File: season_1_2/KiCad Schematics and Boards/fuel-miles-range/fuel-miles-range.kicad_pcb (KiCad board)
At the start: 2 copper layers, 132 x 76 mm, 18 parts, among them J601 Conn_02x06_Top_Bottom, U501 TLC5957RTQ, U502 TLC5957RTQ, U601 MCP2562-E-SN, U602 STM32G0B1CET6N

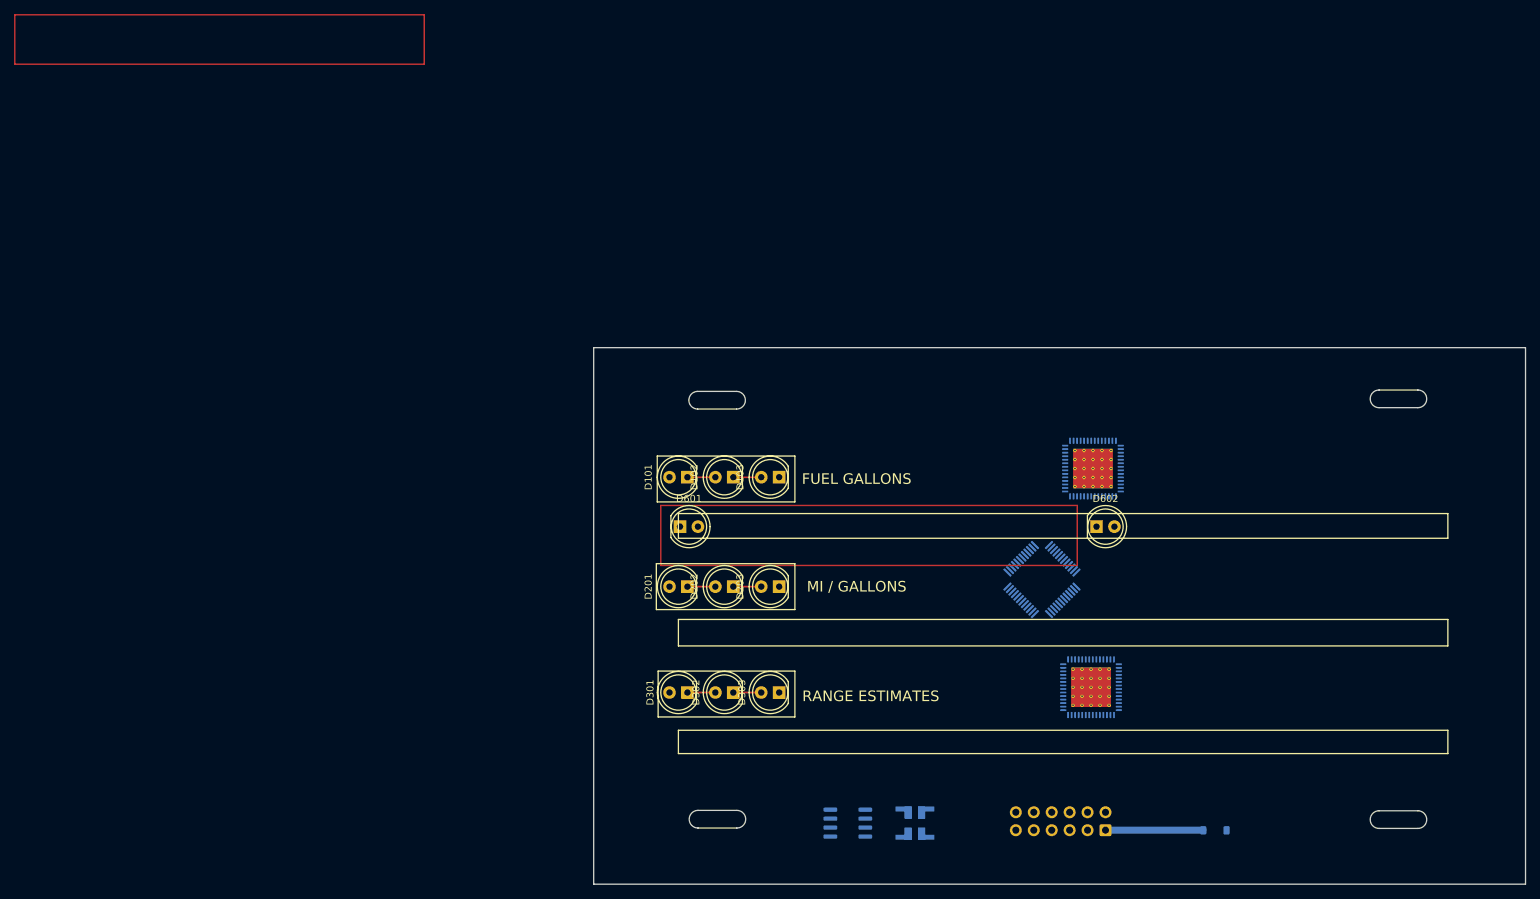
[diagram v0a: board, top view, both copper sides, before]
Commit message: Added lots of electronic devices and routes
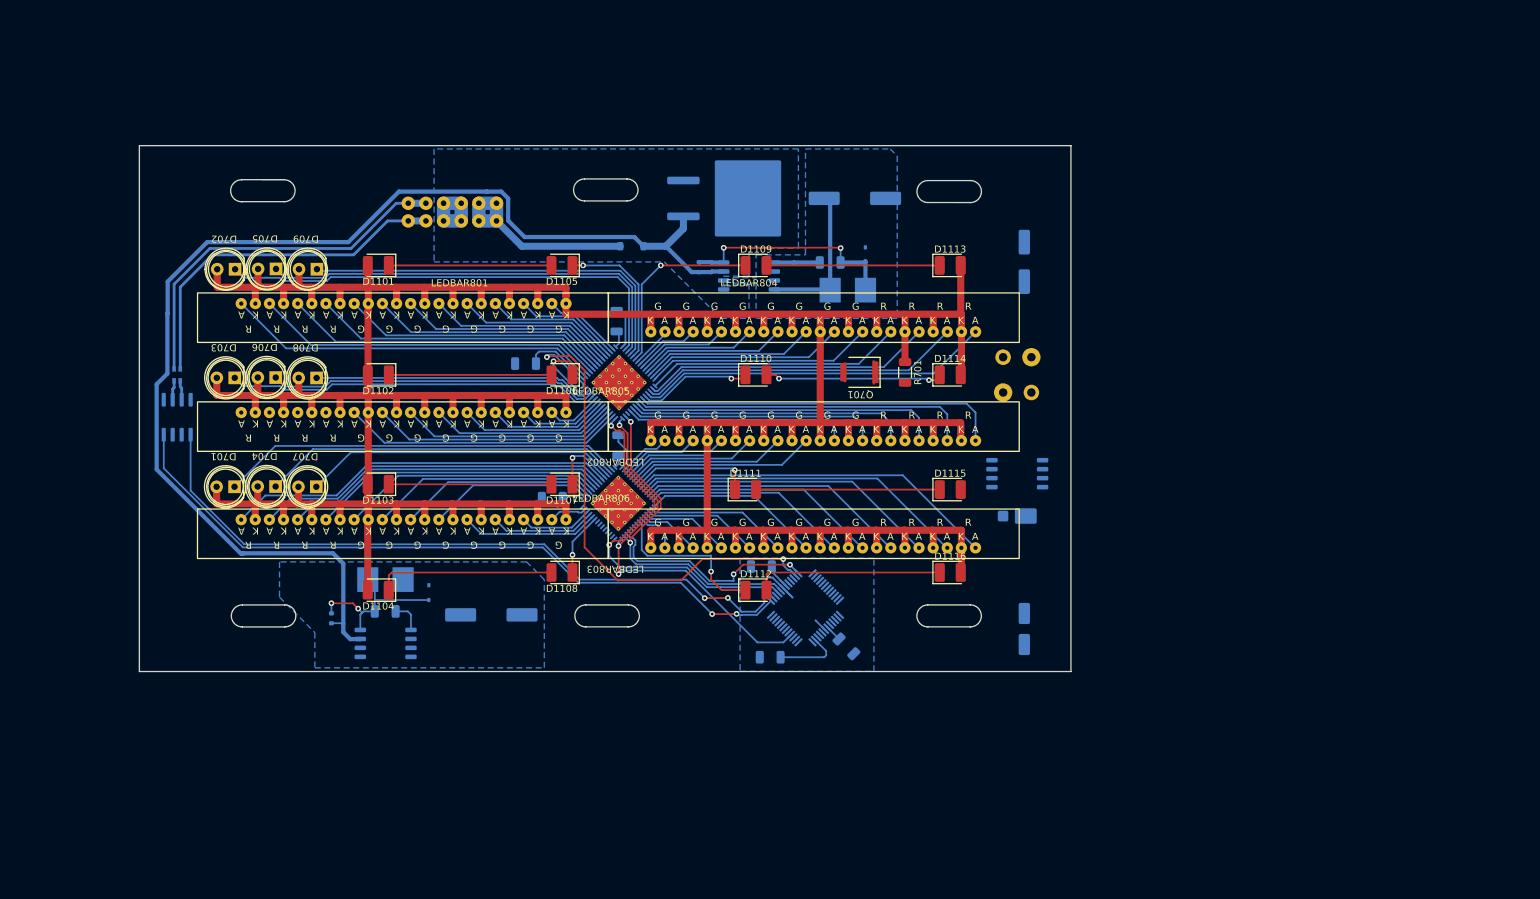
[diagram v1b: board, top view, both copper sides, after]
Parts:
- removed D601, D602: LED, LED_THT:LED_D5.0mm
- removed D603: SM8S24AHE3_A/I, Diode_SMD:D_SOD-123
- removed J601: Conn_02x06_Top_Bottom, Connector_IDC:IDC-Header_2x06_P2.54mm_Vertical
- removed the U501 at (152.7, 64.3)
- removed U502: TLC5957RTQ, Package_DFN_QFN:QFN-56-1EP_8x8mm_P0.5mm_EP5.6x5.6mm_ThermalVias
- added C203: 0.01µF/50V, Capacitor_SMD:C_1206_3216Metric, B.Cu at (115.5, 35.1)
- added C206: 47µF/6,3V, Capacitor_SMD:CP_Elec_10x12.6, B.Cu at (119.0, 26.0)
- added C301: 0.01µF/50V, Capacitor_SMD:C_1206_3216Metric, B.Cu at (52.5, 84.5)
- added C303: 100µF/6,3V, Capacitor_SMD:CP_Elec_10x12.6, B.Cu at (67.5, 85.0)
- added C401: 10µF/25V, Capacitor_SMD:CP_Elec_6.3x5.9, B.Cu at (143.0, 35.0)
- added C402: 47µF/6,3V, Capacitor_SMD:CP_Elec_5x5.7, B.Cu at (143.0, 87.0)
- added C501: 100n, Capacitor_SMD:C_1206_3216Metric, B.Cu at (117.8, 89.5)
- added C502: 100n, Capacitor_SMD:C_1206_3216Metric, B.Cu at (105.8, 78.2)
- added C503: 100n, Capacitor_SMD:C_1206_3216Metric, B.Cu at (107.0, 91.0)
- added C901: 100n, Capacitor_SMD:C_1206_3216Metric, B.Cu at (72.3, 49.4)
- added C902: 100n, Capacitor_SMD:C_1206_3216Metric, B.Cu at (76.1, 68.5)
- added D1101: LED, LED_SMD:LED_1210_3225Metric_Pad1.42x2.65mm_HandSolder, F.Cu at (51.5, 35.5)
- added D1102: LED, LED_SMD:LED_1210_3225Metric_Pad1.42x2.65mm_HandSolder, F.Cu at (51.5, 51.0)
- added D1103: LED, LED_SMD:LED_1210_3225Metric_Pad1.42x2.65mm_HandSolder, F.Cu at (51.5, 66.5)
- added D1104: LED, LED_SMD:LED_1210_3225Metric_Pad1.42x2.65mm_HandSolder, F.Cu at (51.5, 81.5)
- added D1105: LED, LED_SMD:LED_1210_3225Metric_Pad1.42x2.65mm_HandSolder, F.Cu at (77.5, 35.5)
- added D1106: LED, LED_SMD:LED_1210_3225Metric_Pad1.42x2.65mm_HandSolder, F.Cu at (77.5, 51.0)
- added D1107: LED, LED_SMD:LED_1210_3225Metric_Pad1.42x2.65mm_HandSolder, F.Cu at (77.5, 66.5)
- added D1108: LED, LED_SMD:LED_1210_3225Metric_Pad1.42x2.65mm_HandSolder, F.Cu at (77.5, 79.0)
- added D1109: LED, LED_SMD:LED_1210_3225Metric_Pad1.42x2.65mm_HandSolder, F.Cu at (105.0, 35.5)
- added D1110: LED, LED_SMD:LED_1210_3225Metric_Pad1.42x2.65mm_HandSolder, F.Cu at (105.0, 51.0)
- added D1111: LED, LED_SMD:LED_1210_3225Metric_Pad1.42x2.65mm_HandSolder, F.Cu at (103.5, 67.2)
- added D1112: LED, LED_SMD:LED_1210_3225Metric_Pad1.42x2.65mm_HandSolder, F.Cu at (105.0, 81.5)
- added D1113: LED, LED_SMD:LED_1210_3225Metric_Pad1.42x2.65mm_HandSolder, F.Cu at (132.5, 35.5)
- added D1114: LED, LED_SMD:LED_1210_3225Metric_Pad1.42x2.65mm_HandSolder, F.Cu at (132.5, 51.0)
- added D1115: LED, LED_SMD:LED_1210_3225Metric_Pad1.42x2.65mm_HandSolder, F.Cu at (132.5, 67.2)
- added D1116: LED, LED_SMD:LED_1210_3225Metric_Pad1.42x2.65mm_HandSolder, F.Cu at (132.5, 79.0)
- added D204: SMBJ22A, Diode_SMD:D_SOD-123, B.Cu at (87.4, 32.8)
- added D205: LDP01-30AY, Package_TO_SOT_SMD:TO-263-2, B.Cu at (102.4, 26.0)
- added D206: 1N4148, Diode_SMD:D_SOD-523, B.Cu at (96.9, 35.7)
- added D207: 3,3A/50V, Diode_SMD:D_SOD-323, B.Cu at (120.5, 34.0)
- added D304: 1N4148, Diode_SMD:D_SOD-523, B.Cu at (44.9, 85.5)
- added D305: 3,3A/50V, Diode_SMD:D_SOD-323, B.Cu at (58.6, 81.8)
- added D401: 3,3A/50V, Diode_SMD:Vishay_SMPA, B.Cu at (142.0, 71.0)
- added L202: 68µH, Inductor_SMD:L_Murata_LQH55DN_5.7x5.0mm, B.Cu at (118.0, 39.0)
- added L301: 100µH, Inductor_SMD:L_Murata_LQH55DN_5.7x5.0mm, B.Cu at (52.5, 80.0)
- added L401: 47µH, Inductor_THT:L_Radial_D10.5mm_P4.00x5.00mm_Murata_1200RS, B.Cu at (144.0, 48.5)
- added LEDBAR801: ~, Code99_LED:LEDBAR_12LED_24PIN, F.Cu at (84.1, 46.4)
- added LEDBAR802: ~, Code99_LED:LEDBAR_12LED_24PIN, F.Cu at (84.1, 61.8)
- added LEDBAR803: ~, Code99_LED:LEDBAR_12LED_24PIN, F.Cu at (84.1, 77.0)
- added LEDBAR804: ~, Code99_LED:LEDBAR_12LED_24PIN, F.Cu at (84.1, 39.4)
- added LEDBAR805: ~, Code99_LED:LEDBAR_12LED_24PIN, F.Cu at (84.1, 54.8)
- added LEDBAR806: ~, Code99_LED:LEDBAR_12LED_24PIN, F.Cu at (84.1, 70.0)
- added Q701: 1541411NBA210, OptoDevice:Osram_SFH2201, F.Cu at (119.6, 50.6)
- added R701: 4k3, Resistor_SMD:R_1206_3216Metric, F.Cu at (126.1, 50.7)
- added R901: 4k3, Resistor_SMD:R_1206_3216Metric, B.Cu at (85.5, 61.0)
- added R902: 4k3, Resistor_SMD:R_1206_3216Metric, B.Cu at (85.2, 43.4)
- added U1001: ~, Code99_Conn:TE-967646-1, B.Cu at (76.0, 20.0)
- added U201: LM2671 3.3V, Package_SO:SOIC-8_5.3x5.3mm_P1.27mm, B.Cu at (104.0, 37.0)
- added U301: LM2671 5.0V, Package_SO:SOIC-8_5.3x5.3mm_P1.27mm, B.Cu at (52.5, 89.0)
- added U401: AP1501 5V0, Package_SO:SOIC-8_5.3x5.3mm_P1.27mm, B.Cu at (142.0, 65.0)
- added U901: TLC5957RTQ, Package_DFN_QFN:QFN-56-1EP_8x8mm_P0.5mm_EP5.6x5.6mm_ThermalVias, B.Cu at (85.5, 69.2)
- added U902: TLC5957RTQ, Package_DFN_QFN:QFN-56-1EP_8x8mm_P0.5mm_EP5.6x5.6mm_ThermalVias, B.Cu at (85.6, 52.1)
- D701: renamed from D301; footprint LED_THT:LED_D5.0mm -> Code99_LED:LED_5MM_YELLOW_DIFF
- D702: renamed from D101; footprint LED_THT:LED_D5.0mm -> Code99_LED:LED_5MM_YELLOW_DIFF
- D703: renamed from D201; footprint LED_THT:LED_D5.0mm -> Code99_LED:LED_5MM_YELLOW_DIFF
- D704: renamed from D302; footprint LED_THT:LED_D5.0mm -> Code99_LED:LED_5MM_YELLOW_DIFF
- D705: renamed from D102; footprint LED_THT:LED_D5.0mm -> Code99_LED:LED_5MM_YELLOW_DIFF
- D706: renamed from D202; footprint LED_THT:LED_D5.0mm -> Code99_LED:LED_5MM_YELLOW_DIFF
- D707: renamed from D303; footprint LED_THT:LED_D5.0mm -> Code99_LED:LED_5MM_YELLOW_DIFF
- D708: renamed from D203; footprint LED_THT:LED_D5.0mm -> Code99_LED:LED_5MM_YELLOW_DIFF
- D709: renamed from D103; footprint LED_THT:LED_D5.0mm -> Code99_LED:LED_5MM_YELLOW_DIFF
- FL601: footprint Inductor_SMD:L_CommonModeChoke_Murata_DLW5BTMxxxSQ2x_5x5mm -> Inductor_SMD:L_CommonModeChoke_Coilcraft_0805USB
- moved FL601 122.3 mm to (23.0, 51.0), turned to 180 degrees
- moved U601 111.0 mm to (23.0, 57.0), turned to 90 degrees
- moved D708 75.4 mm to (41.2, 46.6)
- moved D709 75.3 mm to (41.2, 31.2)
- moved D707 75.2 mm to (41.2, 62.1)
- moved D706 74.8 mm to (35.4, 46.6)
- moved D705 74.7 mm to (35.4, 31.2)
- moved D704 74.6 mm to (35.4, 62.0)
- moved D703 74.1 mm to (29.6, 46.6)
- moved D702 74.0 mm to (29.6, 31.2)
- moved D701 74.0 mm to (29.6, 62.1)
- moved U501 33.7 mm to (112.0, 84.0)
- renumbered U602 to U501
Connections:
- net Net-(U602-VSS-Pad30) renamed GND_MCU
- D701 pad 1: Net-(D301-K) -> RANGE-YELLOW-1
- D701 pad 2: Net-(D301-A) -> 9V0
- D702 pad 1: Net-(D101-K) -> FUEL-GALLONS-YELLOW-1
- D702 pad 2: Net-(D101-A) -> 9V0
- D703 pad 1: Net-(D201-K) -> MI-GALLONS-YELLOW-1
- D703 pad 2: Net-(D201-A) -> 9V0
- D704 pad 1: Net-(D302-K) -> RANGE-YELLOW-2
- D704 pad 2: Net-(D301-K) -> 9V0
- D705 pad 1: Net-(D102-K) -> FUEL-GALLONS-YELLOW-2
- D705 pad 2: Net-(D101-K) -> 9V0
- D706 pad 1: Net-(D202-K) -> MI-GALLONS-YELLOW-2
- D706 pad 2: Net-(D201-K) -> 9V0
- D707 pad 1: unconnected-(D303-K-Pad1) -> RANGE-YELLOW-3
- D707 pad 2: Net-(D302-K) -> 9V0
- D708 pad 1: unconnected-(D203-K-Pad1) -> MI-GALLONS-YELLOW-3
- D708 pad 2: Net-(D202-K) -> 9V0
- D709 pad 1: unconnected-(D103-K-Pad1) -> FUEL-GALLONS-YELLOW-3
- D709 pad 2: Net-(D102-K) -> 9V0
- FL601 pad 1: Net-(U601-CANH) -> CAN_H
- FL601 pad 2: CAN_H -> Net-(U601-CANH)
- U501 pad 11: unconnected-(U602-PA0-Pad11) -> LIGHT_SENS
- U501 pad 16: unconnected-(U602-PA5-Pad16) -> LED_CTRL_SCLK
- U501 pad 25: unconnected-(U602-PB13-Pad25) -> FDCAN1_RX
- U501 pad 26: unconnected-(U602-PB14-Pad26) -> FDCAN1_TX
- U501 pad 28: unconnected-(U602-PA8-Pad28) -> LED_CTRL_GCLK
- U501 pad 29: unconnected-(U602-PA9/UCPD1_DBCC1-Pad29) -> LED_CTRL_LAT
- U501 pad 31: unconnected-(U602-VDD-Pad31) -> 3V3
- U501 pad 35: unconnected-(U602-PA13-Pad35) -> LED_CONTROLLER_LAST_OUT
- U501 pad 36: unconnected-(U602-PA14-Pad36) -> LED_CONTROLLER_DATA
- U501 pad 6: unconnected-(U602-VDD-Pad6) -> 3V3
- U601 pad 1: CAN_TXD -> FDCAN1_TX
- U601 pad 4: CAN_RXD -> FDCAN1_RX
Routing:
- net 9V0: track 0.00 -> 577.5 mm
- net COMMON_VIN: track 0.00 -> 169.4 mm
- net FDCAN1_RX: track 0.00 -> 100.2 mm, vias 0 -> 2
- net FDCAN1_TX: track 0.00 -> 99.4 mm, vias 0 -> 2
- net LED_CONTROLLER_LAST_OUT: track 0.00 -> 73.2 mm, vias 0 -> 2
- net FUEL-GALLONS-YELLOW-1: track 0.00 -> 66.2 mm
- net FUEL-GALLONS-YELLOW-2: track 0.00 -> 61.4 mm
- net RANGE-YELLOW-1: track 0.00 -> 57.3 mm
- net LED_CTRL_SCLK: track 0.00 -> 57.2 mm, vias 0 -> 3
- net FUEL-GALLONS-YELLOW-3: track 0.00 -> 56.1 mm
- net LED BAR 5 LED RD 4: track 0.00 -> 55.5 mm
- net MI-GALLONS-YELLOW-1: track 0.00 -> 53.2 mm
- net LED_CTRL_GCLK: track 0.00 -> 53.1 mm, vias 0 -> 2
- net LED BAR 1 LED RD 4: track 0.00 -> 53.1 mm
- net CAN_H: track 0.00 -> 52.4 mm
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- added copper zone on B.Cu, net GND_3V3
- added copper zone on B.Cu, net GND_5V0
- added copper zone on B.Cu, net GND_MCU
- added copper zone on B.Cu, net GND_VEHICLE
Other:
- board size 132 x 76 mm -> 132 x 74.5 mm
- board text removed: "FUEL GALLONS"
- board text removed: "MI / GALLONS"
- board text removed: "RANGE ESTIMATES"

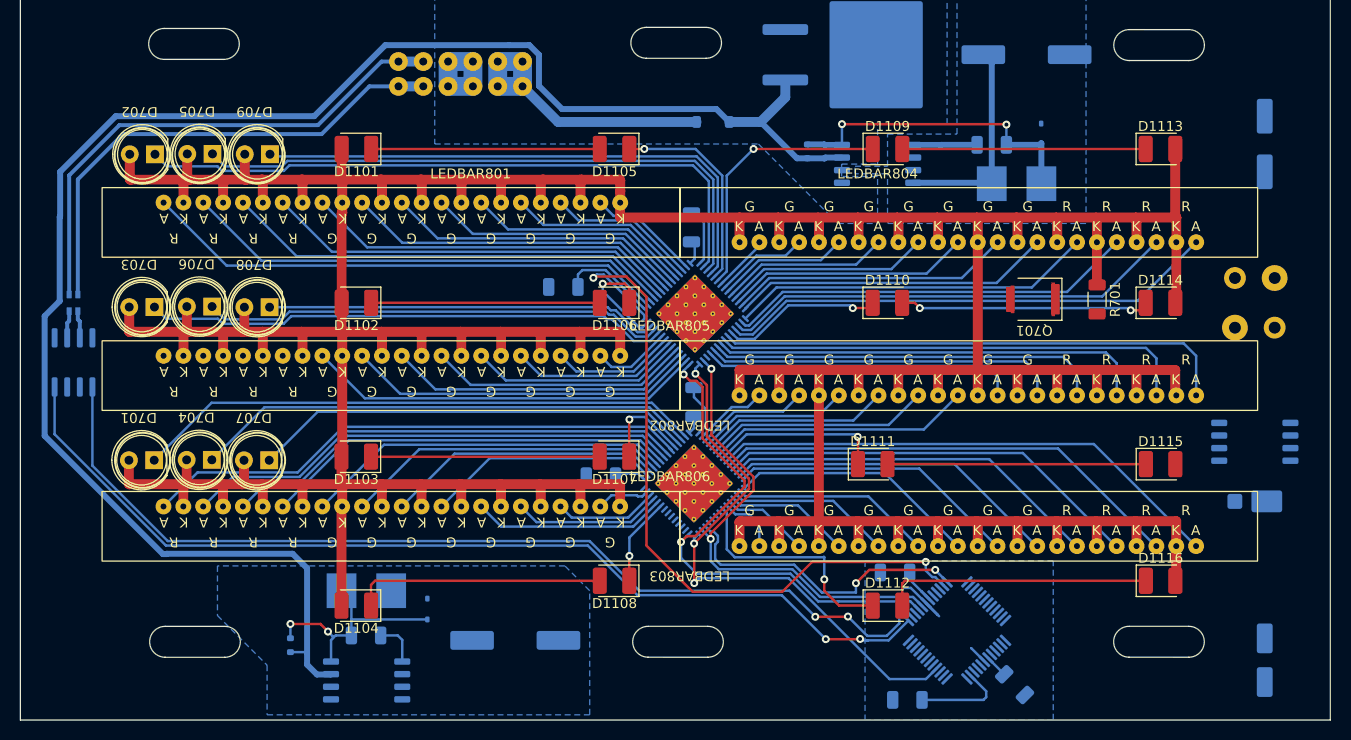
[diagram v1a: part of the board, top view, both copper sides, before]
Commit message: Added 4 missing wires for LED BAR 3, added programming PINs for STM32
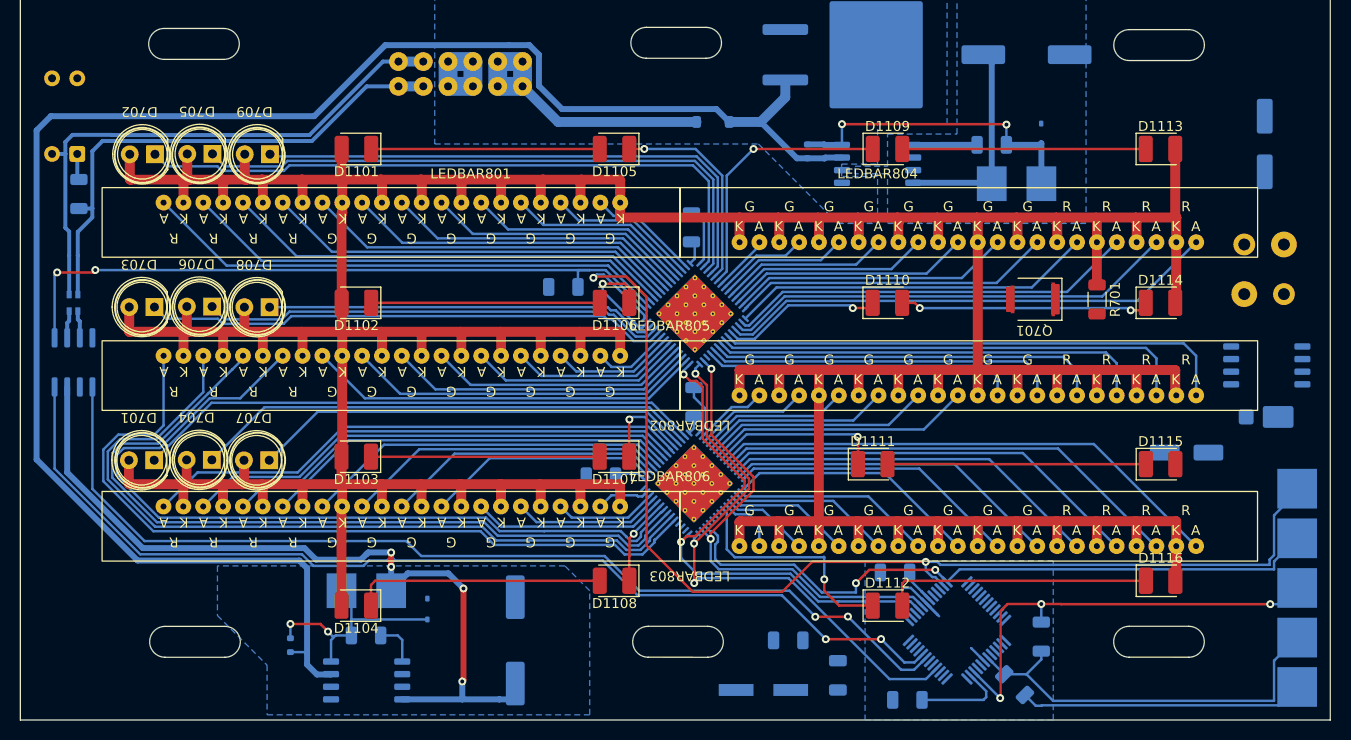
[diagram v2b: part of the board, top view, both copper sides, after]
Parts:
- added C1101: 100n, Capacitor_SMD:C_1206_3216Metric, B.Cu at (95.0, 85.0)
- added C1102: 100n, Capacitor_SMD:C_1206_3216Metric, B.Cu at (100.0, 88.5)
- added J1101: VCC, TestPoint:TestPoint_Pad_4.0x4.0mm, B.Cu at (146.3, 84.7)
- added J1102: NRST, TestPoint:TestPoint_Pad_4.0x4.0mm, B.Cu at (146.3, 79.7)
- added J1103: SWCLK, TestPoint:TestPoint_Pad_4.0x4.0mm, B.Cu at (146.3, 74.7)
- added J1104: SWDIO, TestPoint:TestPoint_Pad_4.0x4.0mm, B.Cu at (146.3, 69.7)
- added J1105: GND, TestPoint:TestPoint_Pad_4.0x4.0mm, B.Cu at (146.3, 89.7)
- added R1101: 120R, Resistor_SMD:R_1206_3216Metric, B.Cu at (23.5, 40.0)
- added R1102: 10k, Resistor_SMD:R_1206_3216Metric, B.Cu at (120.5, 84.6)
- added SW1101: SW_DIP_x01, Package_DIP:DIP-4_W7.62mm, B.Cu at (23.4, 36.0)
- added Y1101: 16000000, Crystal:Crystal_SMD_ECS_CSM3X-2Pin_7.6x4.1mm, B.Cu at (92.5, 90.0)
- moved C402 22.3 mm to (135.1, 66.1), turned to 180 degrees
- moved D401 8.58 mm to (143.1, 62.5)
- moved U401 7.79 mm to (143.2, 57.3), turned to 0 degrees
- moved L401 3.51 mm to (144.9, 45.1)
- turned C303 to 90 degrees
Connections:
- U1001 pad 11: CAN_H -> CAN_L
- U1001 pad 12: CAN_H -> CAN_L
- U1001 pad 5: CAN_L -> CAN_H
- U1001 pad 6: CAN_L -> CAN_H
- U501 pad 10: unconnected-(U501-PF2-Pad10) -> Net-(J1102-Pin_1)
- U501 pad 19: unconnected-(U501-PB0-Pad19) -> FDCAN1_RX
- U501 pad 20: unconnected-(U501-PB1-Pad20) -> FDCAN1_TX
- U501 pad 25: FDCAN1_RX -> unconnected-(U501-PB13-Pad25)
- U501 pad 26: FDCAN1_TX -> unconnected-(U501-PB14-Pad26)
- U501 pad 8: unconnected-(U501-PF0-Pad8) -> Net-(U501-PF0)
- U501 pad 9: unconnected-(U501-PF1-Pad9) -> Net-(U501-PF1)
- U601 pad 1: FDCAN1_TX -> FDCAN1_RX
- U601 pad 4: FDCAN1_RX -> FDCAN1_TX
- U901 pad 33: unconnected-(U901-OUTR7-Pad33) -> LED BAR 3 LED RD 4
- U901 pad 34: unconnected-(U901-OUTG7-Pad34) -> LED BAR 3 LED RD 3
- U901 pad 35: unconnected-(U901-OUTB7-Pad35) -> LED BAR 3 LED RD 2
- U901 pad 36: unconnected-(U901-OUTR8-Pad36) -> LED BAR 3 LED RD 1
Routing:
- net 3V3: track 41.1 -> 140.4 mm, vias 0 -> 2
- net LED BAR 3 LED RD 1: track 0.00 -> 82.4 mm
- net 5V0: track 0.00 -> 81.8 mm, vias 0 -> 4
- net LED BAR 3 LED RD 2: track 0.00 -> 80.5 mm
- net LED BAR 3 LED RD 3: track 0.00 -> 79.8 mm
- net LED BAR 3 LED RD 4: track 0.00 -> 79.5 mm
- net Net-(J1102-Pin_1): track 0.00 -> 45.2 mm, vias 0 -> 3
- net LED_CONTROLLER_LAST_OUT: track 73.2 -> 116.8 mm
- net LED_CONTROLLER_DATA: track 30.8 -> 68.4 mm
- net GND_MCU: track 8.36 -> 37.0 mm
- net COMMON_VIN: track 169.4 -> 175.7 mm
- net CAN_L: track 50.3 -> 56.4 mm
- net FDCAN1_TX: track 99.4 -> 104.6 mm
- net Net-(R1101-Pad1): track 0.00 -> 2.64 mm
- net FDCAN1_RX: track 100.2 -> 102.3 mm
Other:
- board text added: "3V3"
- board text added: "CAN"
- board text added: "GND"
- board text added: "NRST"
- board text added: "OFF"
- board text added: "ON"
- board text added: "SWCLK"
- board text added: "SWDIO"
- board text added: "TERM"
